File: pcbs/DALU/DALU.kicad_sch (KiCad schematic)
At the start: 0 parts

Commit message: More rerouting
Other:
- sheet AdderSubtractor ports: added RESULT[0..7]; removed none
- sheet NAND ports: added RESULT[0..7], ~{NAND}; removed none
- sheet OR ports: added RESULT[0..7]; removed none
- sheet Output Stage ports: added COMMIT, DALUFLAG, DECODE, EXECUTE, FLAG, RESULT[0..7]; removed none
- sheet XOR ports: added RESULT[0..7]; removed none
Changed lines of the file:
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@@
   (junction (at 184.15 97.79) (diameter 0) (color 0 0 0 0)
   )
+  (junction (at 225.425 82.55) (diameter 0) (color 0 0 0 0)
+  )
+  (junction (at 225.425 107.95) (diameter 0) (color 0 0 0 0)
+  )
+  (junction (at 225.425 59.69) (diameter 0) (color 0 0 0 0)
+  )
   (junction (at 180.34 46.99) (diameter 0) (color 0 0 0 0)
   )
-  (junction (at 180.34 80.645) (diameter 0) (color 0 0 0 0)
-  )
   (junction (at 184.15 57.15) (diameter 0) (color 0 0 0 0)
   )
+  (junction (at 180.34 80.01) (diameter 0) (color 0 0 0 0)
+  )
   (junction (at 180.34 101.6) (diameter 0) (color 0 0 0 0)
   )
@@
   (junction (at 180.34 62.23) (diameter 0) (color 0 0 0 0)
   )
-  (junction (at 184.15 77.47) (diameter 0) (color 0 0 0 0)
-  )
-  (bus (pts (xy 180.34 62.23) (xy 180.34 80.645))
-    (stroke (width 0) (type default) (color 0 0 0 0))
-  )
-  (bus (pts (xy 180.34 80.645) (xy 180.34 101.6))
-    (stroke (width 0) (type default) (color 0 0 0 0))
-  )
-  (bus (pts (xy 180.34 80.645) (xy 189.23 80.645))
+  (junction (at 220.98 59.69) (diameter 0) (color 0 0 0 0)
+  )
+  (junction (at 184.15 76.835) (diameter 0) (color 0 0 0 0)
+  )
+  (bus (pts (xy 180.34 62.23) (xy 180.34 80.01))
+    (stroke (width 0) (type default) (color 0 0 0 0))
+  )
+  (bus (pts (xy 208.28 59.69) (xy 220.98 59.69))
+    (stroke (width 0) (type default) (color 0 0 0 0))
+  )
+  (bus (pts (xy 225.425 59.69) (xy 232.41 59.69))
     (stroke (width 0) (type default) (color 0 0 0 0))
   )
@@
     (stroke (width 0) (type default) (color 0 0 0 0))
   )
-  (bus (pts (xy 184.15 77.47) (xy 189.23 77.47))
-    (stroke (width 0) (type default) (color 0 0 0 0))
-  )
-  (bus (pts (xy 184.15 57.15) (xy 184.15 77.47))
-    (stroke (width 0) (type default) (color 0 0 0 0))
-  )
-  (bus (pts (xy 184.15 77.47) (xy 184.15 97.79))
+  (bus (pts (xy 220.98 32.385) (xy 220.98 59.69))
+    (stroke (width 0) (type default) (color 0 0 0 0))
+  )
+  (bus (pts (xy 208.28 82.55) (xy 225.425 82.55))
+    (stroke (width 0) (type default) (color 0 0 0 0))
+  )
+  (bus (pts (xy 208.28 32.385) (xy 220.98 32.385))
+    (stroke (width 0) (type default) (color 0 0 0 0))
+  )
+  (bus (pts (xy 220.98 59.69) (xy 225.425 59.69))
+    (stroke (width 0) (type default) (color 0 0 0 0))
+  )
+  (bus (pts (xy 184.15 57.15) (xy 184.15 76.835))
     (stroke (width 0) (type default) (color 0 0 0 0))
   )
@@
     (stroke (width 0) (type default) (color 0 0 0 0))
   )
+  (bus (pts (xy 184.15 76.835) (xy 184.15 97.79))
+    (stroke (width 0) (type default) (color 0 0 0 0))
+  )
   (bus (pts (xy 93.98 46.99) (xy 180.34 46.99))
     (stroke (width 0) (type default) (color 0 0 0 0))
   )
+  (bus (pts (xy 225.425 130.81) (xy 225.425 107.95))
+    (stroke (width 0) (type default) (color 0 0 0 0))
+  )
   (bus (pts (xy 184.15 40.64) (xy 184.15 35.56))
     (stroke (width 0) (type default) (color 0 0 0 0))
   )
+  (bus (pts (xy 184.15 76.835) (xy 189.23 76.835))
+    (stroke (width 0) (type default) (color 0 0 0 0))
+  )
+  (bus (pts (xy 225.425 107.95) (xy 225.425 82.55))
+    (stroke (width 0) (type default) (color 0 0 0 0))
+  )
+  (bus (pts (xy 180.34 80.01) (xy 180.34 101.6))
+    (stroke (width 0) (type default) (color 0 0 0 0))
+  )
   (bus (pts (xy 189.23 124.46) (xy 184.15 124.46))
     (stroke (width 0) (type default) (color 0 0 0 0))
@@
     (stroke (width 0) (type default) (color 0 0 0 0))
   )
+  (bus (pts (xy 208.28 107.95) (xy 225.425 107.95))
+    (stroke (width 0) (type default) (color 0 0 0 0))
+  )
   (bus (pts (xy 46.99 111.76) (xy 61.595 111.76))
     (stroke (width 0) (type default) (color 0 0 0 0))
@@
     (stroke (width 0) (type default) (color 0 0 0 0))
   )
+  (bus (pts (xy 212.09 130.81) (xy 225.425 130.81))
+    (stroke (width 0) (type default) (color 0 0 0 0))
+  )
   (bus (pts (xy 184.15 57.15) (xy 184.15 40.64))
     (stroke (width 0) (type default) (color 0 0 0 0))
   )
+  (bus (pts (xy 225.425 82.55) (xy 225.425 59.69))
+    (stroke (width 0) (type default) (color 0 0 0 0))
+  )
   (bus (pts (xy 180.34 62.23) (xy 180.34 46.99))
     (stroke (width 0) (type default) (color 0 0 0 0))
@@
     (stroke (width 0) (type default) (color 0 0 0 0))
   )
+  (bus (pts (xy 180.34 80.01) (xy 189.23 80.01))
+    (stroke (width 0) (type default) (color 0 0 0 0))
+  )
   (bus (pts (xy 189.23 39.37) (xy 180.34 39.37))
     (stroke (width 0) (type default) (color 0 0 0 0))
@@
       (effects (font (size 1.27 1.27)) (justify left top))
     )
-    (pin "A[0..7]" input (at 189.23 77.47 180)
-      (effects (font (size 1.27 1.27)) (justify left))
-    )
-    (pin "B[0..7]" input (at 189.23 80.645 180)
-      (effects (font (size 1.27 1.27)) (justify left))
-    )
-    (pin "~{XOR}" input (at 189.23 84.455 180)
-      (effects (font (size 1.27 1.27)) (justify left))
+    (pin "A[0..7]" input (at 189.23 76.835 180)
+      (effects (font (size 1.27 1.27)) (justify left))
+    )
+    (pin "B[0..7]" input (at 189.23 80.01 180)
+      (effects (font (size 1.27 1.27)) (justify left))
+    )
+    (pin "~{XOR}" input (at 189.23 85.09 180)
+      (effects (font (size 1.27 1.27)) (justify left))
+    )
+    (pin "RESULT[0..7]" tri_state (at 208.28 82.55 0)
+      (effects (font (size 1.27 1.27)) (justify right))
     )
   )
@@
     )
   )
-  (sheet (at 189.23 33.02) (size 19.05 13.97) (fields_autoplaced)
-    (stroke (width 0.1524) (type solid) (color 0 0 0 0))
-    (fill (color 0 0 0 0.0000))
-    (property "Sheet name" "AdderSubtractor" (id 0) (at 189.23 32.3084 0)
+  (sheet (at 189.23 29.845) (size 19.05 17.145) (fields_autoplaced)
+    (stroke (width 0.1524) (type solid) (color 0 0 0 0))
+    (fill (color 0 0 0 0.0000))
+    (property "Sheet name" "AdderSubtractor" (id 0) (at 189.23 29.1334 0)
       (effects (font (size 1.27 1.27)) (justify left bottom))
     )
@@
       (effects (font (size 1.27 1.27)) (justify left))
     )
-    (pin "FLAG" output (at 208.28 35.56 0)
+    (pin "FLAG" output (at 208.28 40.005 0)
       (effects (font (size 1.27 1.27)) (justify right))
     )
@@
       (effects (font (size 1.27 1.27)) (justify left))
     )
+    (pin "RESULT[0..7]" tri_state (at 208.28 32.385 0)
+      (effects (font (size 1.27 1.27)) (justify right))
+    )
   )
   (sheet (at 189.23 93.98) (size 19.05 17.145) (fields_autoplaced)
@@
       (effects (font (size 1.27 1.27)) (justify left))
     )
+    (pin "RESULT[0..7]" tri_state (at 208.28 107.95 0)
+      (effects (font (size 1.27 1.27)) (justify right))
+    )
   )
   (sheet (at 232.41 44.45) (size 44.45 46.99) (fields_autoplaced)
@@
       (effects (font (size 1.27 1.27)) (justify left top))
     )
+    (pin "DALUFLAG" output (at 276.86 49.53 0)
+      (effects (font (size 1.27 1.27)) (justify right))
+    )
+    (pin "FLAG" input (at 232.41 48.895 180)
+      (effects (font (size 1.27 1.27)) (justify left))
+    )
+    (pin "EXECUTE" input (at 232.41 87.63 180)
+      (effects (font (size 1.27 1.27)) (justify left))
+    )
+    (pin "DECODE" input (at 232.41 85.09 180)
+      (effects (font (size 1.27 1.27)) (justify left))
+    )
+    (pin "COMMIT" input (at 232.41 90.17 180)
+      (effects (font (size 1.27 1.27)) (justify left))
+    )
+    (pin "RESULT[0..7]" input (at 232.41 59.69 180)
+      (effects (font (size 1.27 1.27)) (justify left))
+    )
   )
   (sheet (at 189.23 53.34) (size 19.05 13.97) (fields_autoplaced)
@@
       (effects (font (size 1.27 1.27)) (justify left))
     )
+    (pin "RESULT[0..7]" tri_state (at 208.28 59.69 0)
+      (effects (font (size 1.27 1.27)) (justify right))
+    )
+    (pin "~{NAND}" input (at 189.23 65.405 180)
+      (effects (font (size 1.27 1.27)) (justify left))
+    )

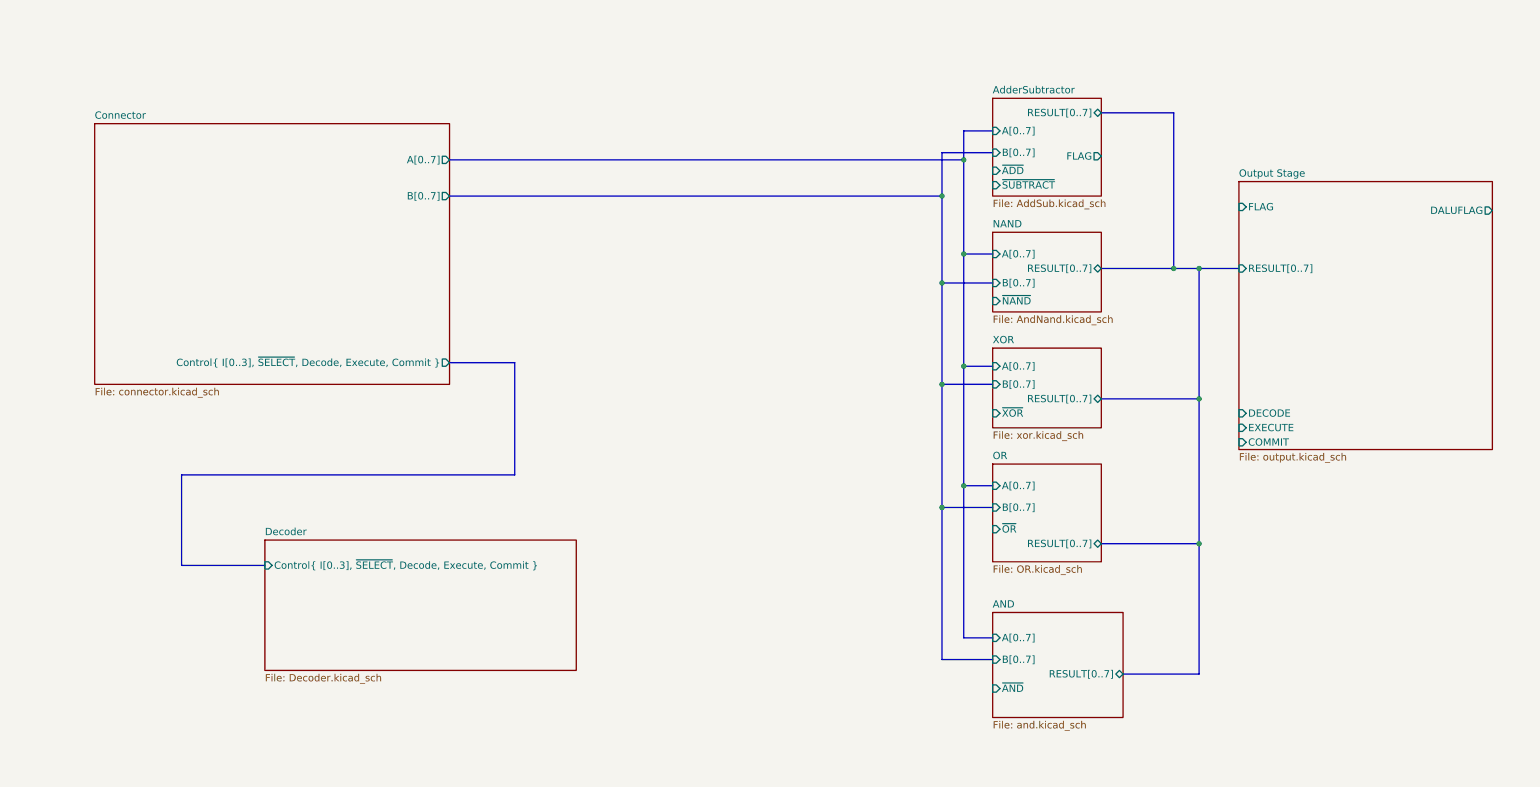
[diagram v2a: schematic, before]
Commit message: Starting to connect up control wires
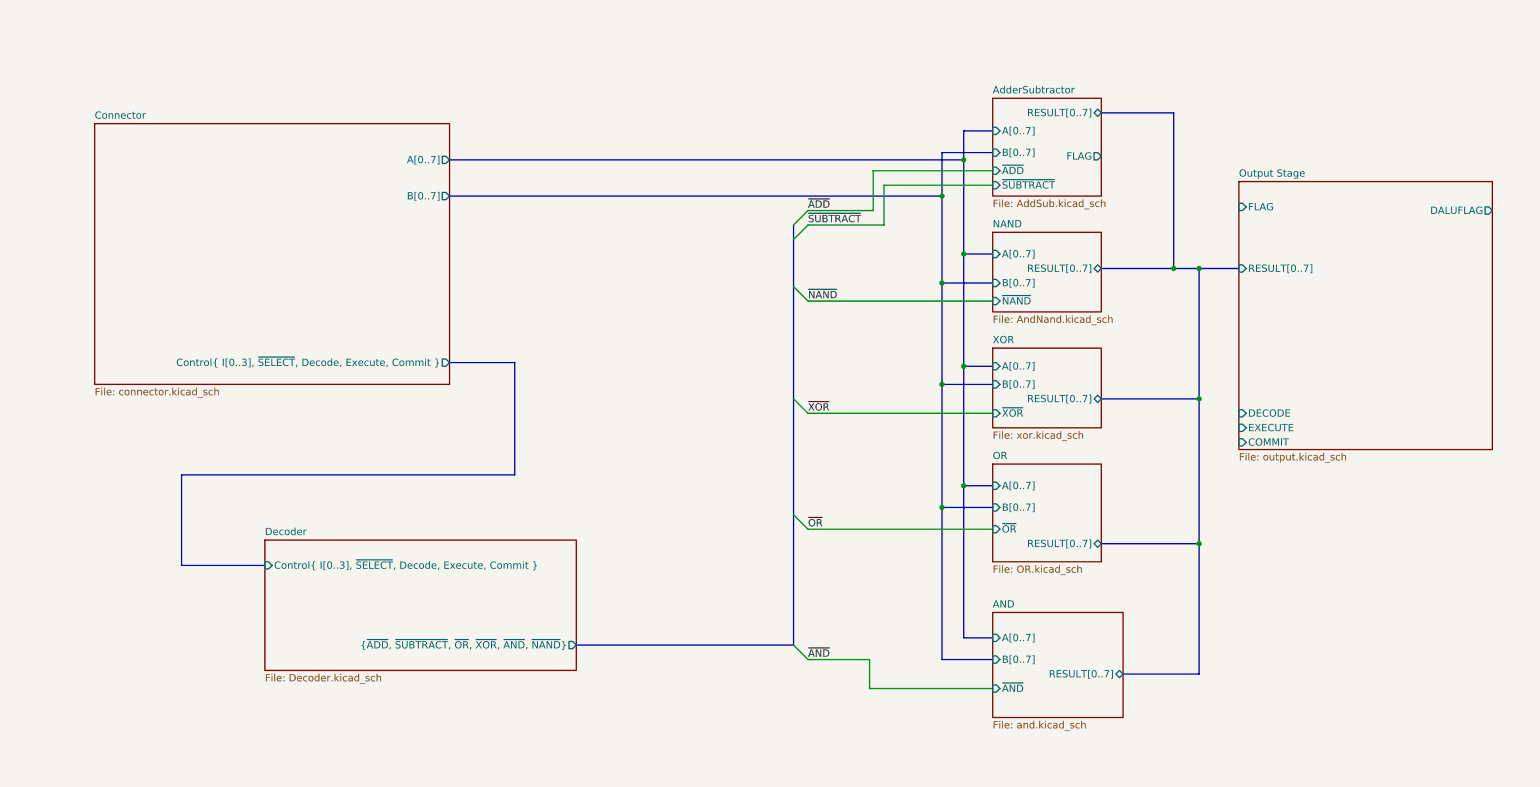
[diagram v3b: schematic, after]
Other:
- sheet Decoder ports: added {~{ADD}, ~{SUBTRACT}, ~{OR}, ~{XOR}, ~{AND}, ~{NAND}}; removed none

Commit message: Finish preliminary routing
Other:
- sheet Connector ports: added C[0..7], DALUFLAG; removed none
- sheet Output Stage ports: added C[0..7]; removed none

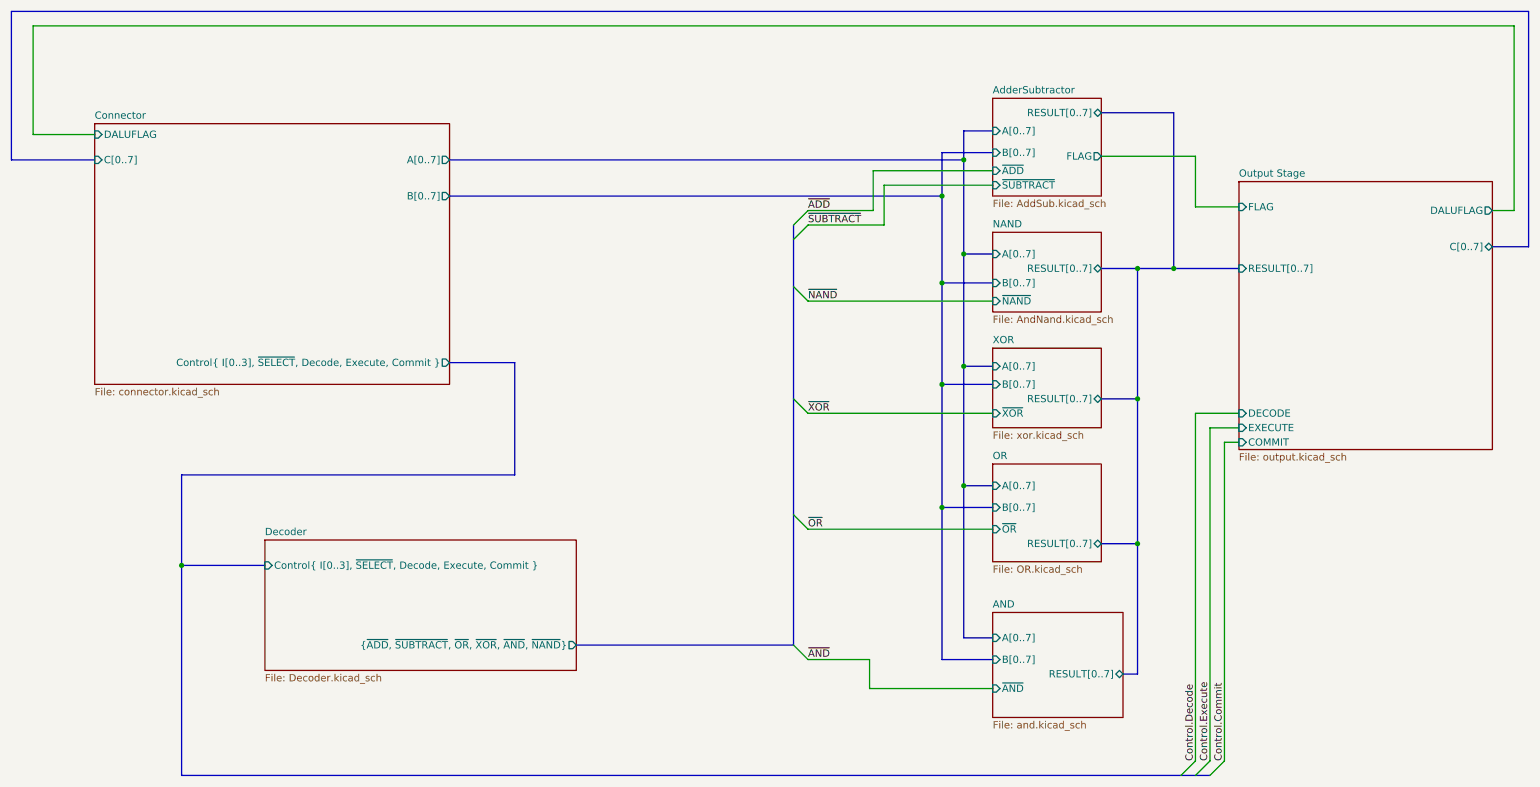
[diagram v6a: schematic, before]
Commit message: Adding test terminals
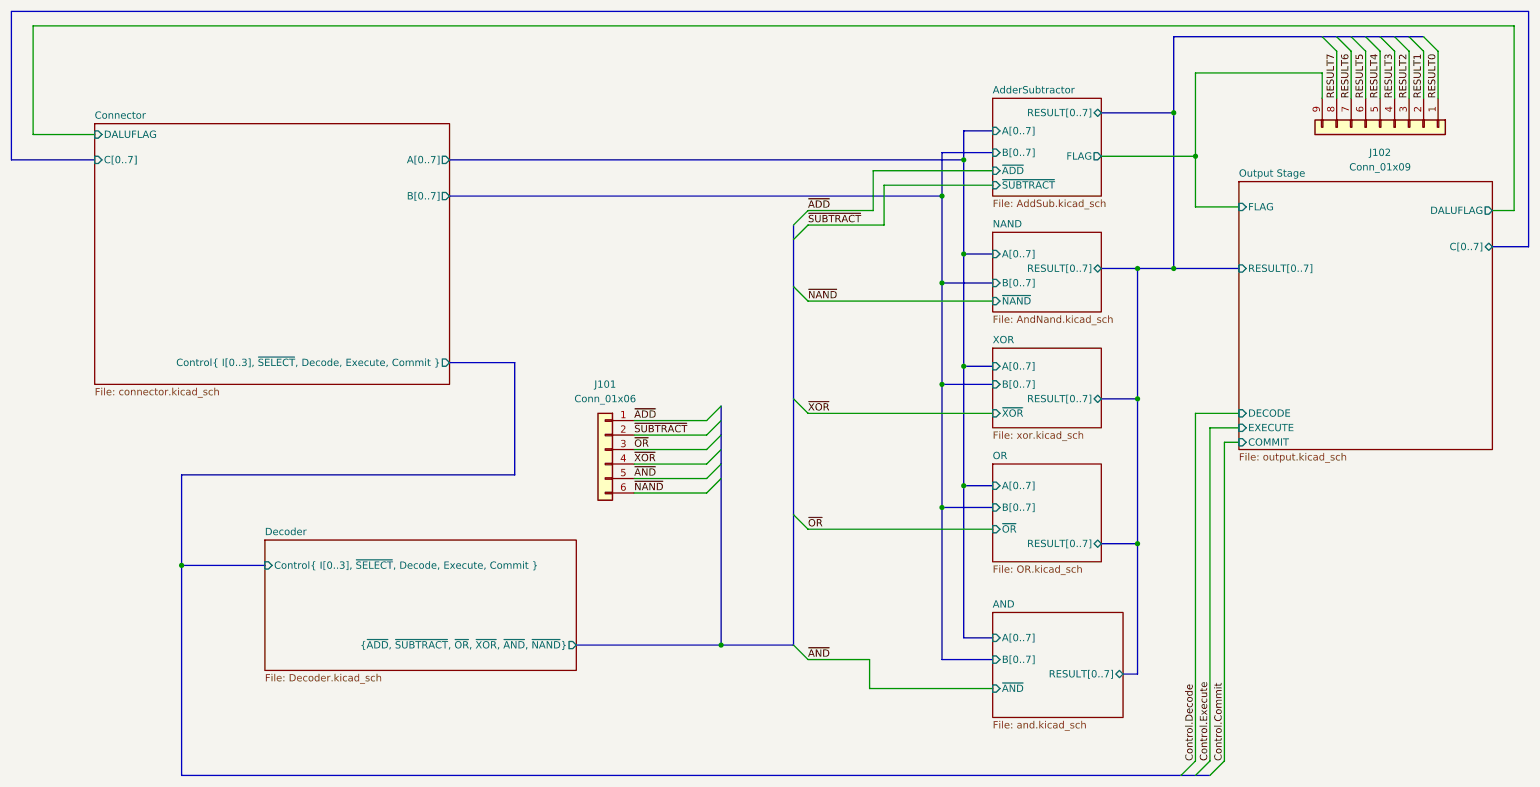
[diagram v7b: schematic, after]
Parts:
- added J101: Conn_01x06, Connector_PinHeader_2.54mm:PinHeader_1x06_P2.54mm_Vertical, symbol Connector_Generic:Conn_01x06
- added J102: Conn_01x09, Connector_PinHeader_2.54mm:PinHeader_1x09_P2.54mm_Vertical, symbol Connector_Generic:Conn_01x09
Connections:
- net AdderSubtractor/FLAG: now also J102.9 (Pin_9)
- net ~{ADD}: now also J101.1 (Pin_1)
- net ~{AND}: now also J101.5 (Pin_5)
- net ~{NAND}: now also J101.6 (Pin_6)
- net ~{OR}: now also J101.3 (Pin_3)
- net ~{SUBTRACT}: now also J101.2 (Pin_2)
- net ~{XOR}: now also J101.4 (Pin_4)
- new net RESULT0: J102.1 (Pin_1)
- new net RESULT1: J102.2 (Pin_2)
- new net RESULT2: J102.3 (Pin_3)
- new net RESULT3: J102.4 (Pin_4)
- new net RESULT4: J102.5 (Pin_5)
- new net RESULT5: J102.6 (Pin_6)
- new net RESULT6: J102.7 (Pin_7)
- new net RESULT7: J102.8 (Pin_8)
